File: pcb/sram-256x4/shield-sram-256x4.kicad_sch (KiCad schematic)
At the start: 24 parts, among them U1 IS61WV25616-10TLI, U2 IS61WV25616-10TLI, U3 IS61WV25616-10TLI, U4 IS61WV25616-10TLI

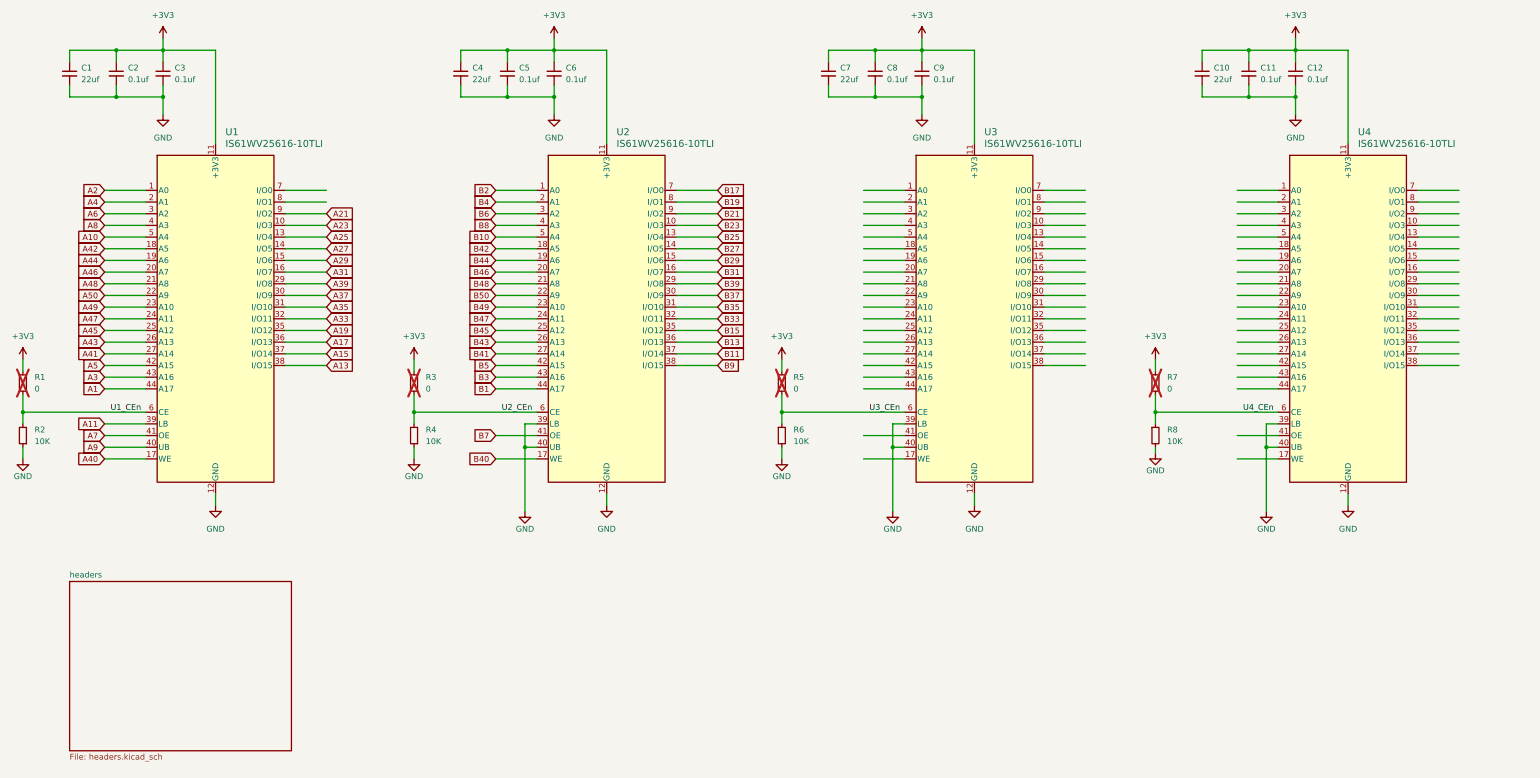
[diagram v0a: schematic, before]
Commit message: [pcb][sram-4x] all but pmod routed for adc board
The sram is doing double duty here during the cross over. It supports
the dfc stacking connector during the transition. It will be removed.
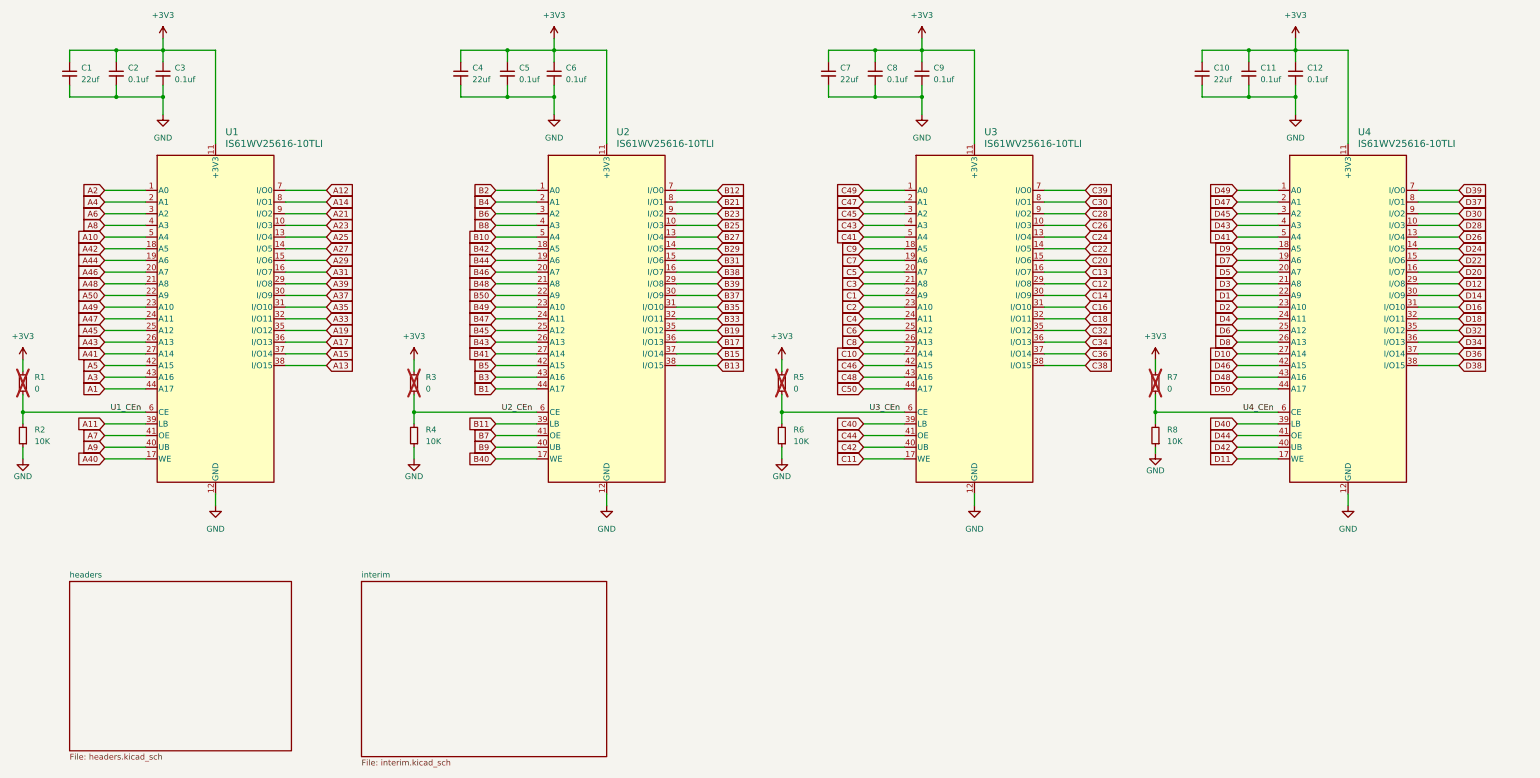
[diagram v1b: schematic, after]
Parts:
- U1, U2, U3, U4: footprint 44L_TSOP-2_400_ISI -> !Misc:44L_TSOP-2_400_ISI
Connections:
- net B11: now also U2.39 (LB); no longer U2.37 (I/O14)
- net B13: now also U2.38 (I/O15); no longer U2.36 (I/O13)
- net B15: now also U2.37 (I/O14); no longer U2.35 (I/O12)
- net B17: now also U2.36 (I/O13); no longer U2.7 (I/O0)
- net B19: now also U2.35 (I/O12); no longer U2.8 (I/O1)
- net B21: now also U2.8 (I/O1); no longer U2.9 (I/O2)
- net B23: now also U2.9 (I/O2); no longer U2.10 (I/O3)
- net B25: now also U2.10 (I/O3); no longer U2.13 (I/O4)
- net B27: now also U2.13 (I/O4); no longer U2.14 (I/O5)
- net B29: now also U2.14 (I/O5); no longer U2.15 (I/O6)
- net B31: now also U2.15 (I/O6); no longer U2.16 (I/O7)
- net B9: now also U2.40 (UB); no longer U2.38 (I/O15)
- net GND: now also R6.1, R8.1; no longer R6.2, R8.2, U2.39 (LB), U2.40 (UB), U3.39 (LB), U3.40 (UB), U4.39 (LB), U4.40 (UB)
- net U3_CEn: now also R6.2; no longer R6.1
- net U4_CEn: now also R8.2; no longer R8.1
- net C49: now reaches U3.1 (A0)
- net C26: now reaches U3.10 (I/O3)
- net C24: now reaches U3.13 (I/O4)
- net C22: now reaches U3.14 (I/O5)
- net C20: now reaches U3.15 (I/O6)
- net C13: now reaches U3.16 (I/O7)
- net C11: now reaches U3.17 (WE)
- net C9: now reaches U3.18 (A5)
- net C7: now reaches U3.19 (A6)
- net C47: now reaches U3.2 (A1)
- net C5: now reaches U3.20 (A7)
- net C3: now reaches U3.21 (A8)
- net C1: now reaches U3.22 (A9)
- net C2: now reaches U3.23 (A10)
- net C4: now reaches U3.24 (A11)
- net C6: now reaches U3.25 (A12)
- net C8: now reaches U3.26 (A13)
- net C10: now reaches U3.27 (A14)
- net C12: now reaches U3.29 (I/O8)
- net C45: now reaches U3.3 (A2)
- net C14: now reaches U3.30 (I/O9)
- net C16: now reaches U3.31 (I/O10)
- net C18: now reaches U3.32 (I/O11)
- net C32: now reaches U3.35 (I/O12)
- net C34: now reaches U3.36 (I/O13)
- net C36: now reaches U3.37 (I/O14)
- net C38: now reaches U3.38 (I/O15)
- net C43: now reaches U3.4 (A3)
- net C44: now reaches U3.41 (OE)
- net C46: now reaches U3.42 (A15)
- net C48: now reaches U3.43 (A16)
- net C50: now reaches U3.44 (A17)
- net C41: now reaches U3.5 (A4)
- net C39: now reaches U3.7 (I/O0)
- net C30: now reaches U3.8 (I/O1)
- net C28: now reaches U3.9 (I/O2)
- net D49: now reaches U4.1 (A0)
- net D28: now reaches U4.10 (I/O3)
- net D26: now reaches U4.13 (I/O4)
- net D24: now reaches U4.14 (I/O5)
- net D22: now reaches U4.15 (I/O6)
- net D20: now reaches U4.16 (I/O7)
- net D11: now reaches U4.17 (WE)
- net D9: now reaches U4.18 (A5)
- net D7: now reaches U4.19 (A6)
- net D47: now reaches U4.2 (A1)
- net D5: now reaches U4.20 (A7)
- net D3: now reaches U4.21 (A8)
- net D1: now reaches U4.22 (A9)
- net D2: now reaches U4.23 (A10)
- net D4: now reaches U4.24 (A11)
- net D6: now reaches U4.25 (A12)
- net D8: now reaches U4.26 (A13)
- net D10: now reaches U4.27 (A14)
- net D12: now reaches U4.29 (I/O8)
- net D45: now reaches U4.3 (A2)
- net D14: now reaches U4.30 (I/O9)
- net D16: now reaches U4.31 (I/O10)
- net D18: now reaches U4.32 (I/O11)
- net D32: now reaches U4.35 (I/O12)
- net D34: now reaches U4.36 (I/O13)
- net D36: now reaches U4.37 (I/O14)
- net D38: now reaches U4.38 (I/O15)
- net D43: now reaches U4.4 (A3)
- net D44: now reaches U4.41 (OE)
- net D46: now reaches U4.42 (A15)
- net D48: now reaches U4.43 (A16)
- net D50: now reaches U4.44 (A17)
- net D41: now reaches U4.5 (A4)
- net D39: now reaches U4.7 (I/O0)
- net D37: now reaches U4.8 (I/O1)
- net D30: now reaches U4.9 (I/O2)
- net A12: now reaches U1.7 (I/O0)
- net A14: now reaches U1.8 (I/O1)
- new net B12: U2.7 (I/O0)
- new net B38: U2.16 (I/O7)
- new net C40: U3.39 (LB)
- new net C42: U3.40 (UB)
- new net D40: U4.39 (LB)
- new net D42: U4.40 (UB)
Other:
- added sheet interim (interim.kicad_sch)
- moved on the sheet: R6, R8

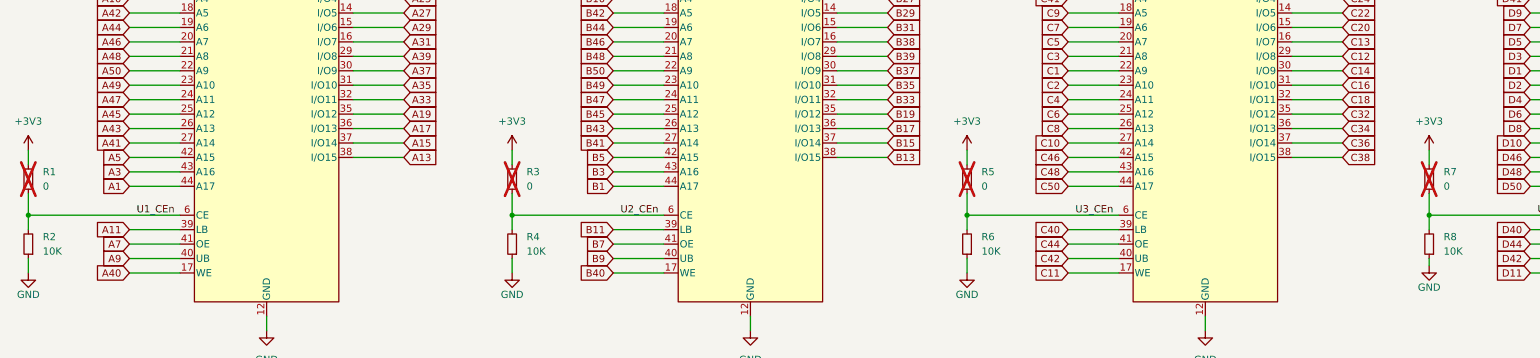
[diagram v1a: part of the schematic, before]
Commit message: [pcb] misc fixes during jlcpcb production submission
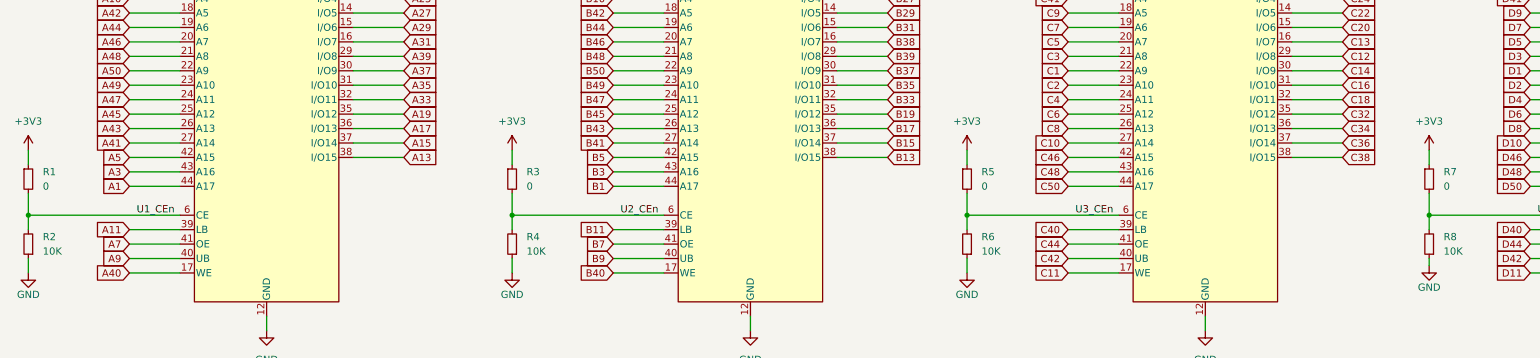
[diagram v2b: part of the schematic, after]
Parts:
- R1, R3, R5, R7: LCSC Part # C21189 -> DNP; now fitted
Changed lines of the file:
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@@
 		(in_bom yes)
 		(on_board yes)
-		(dnp yes)
+		(dnp no)
 		(fields_autoplaced yes)
 		(property "Reference" "R7"
@@
 			)
 		)
-		(property "LCSC Part #" "C21189"
+		(property "LCSC Part #" "DNP"
 			(at 265.43 100.33 0)
 			(effects
@@
 		(in_bom yes)
 		(on_board yes)
-		(dnp yes)
+		(dnp no)
 		(fields_autoplaced yes)
 		(property "Reference" "R5"
@@
 			)
 		)
-		(property "LCSC Part #" "C21189"
+		(property "LCSC Part #" "DNP"
 			(at 184.15 100.33 0)
 			(effects
@@
 		(in_bom yes)
 		(on_board yes)
-		(dnp yes)
+		(dnp no)
 		(fields_autoplaced yes)
 		(property "Reference" "R1"
@@
 			)
 		)
-		(property "LCSC Part #" "C21189"
+		(property "LCSC Part #" "DNP"
 			(at 19.05 100.33 0)
 			(effects
@@
 		(in_bom yes)
 		(on_board yes)
-		(dnp yes)
+		(dnp no)
 		(fields_autoplaced yes)
 		(property "Reference" "R3"
@@
 			)
 		)
-		(property "LCSC Part #" "C21189"
+		(property "LCSC Part #" "DNP"
 			(at 104.14 100.33 0)
 			(effects

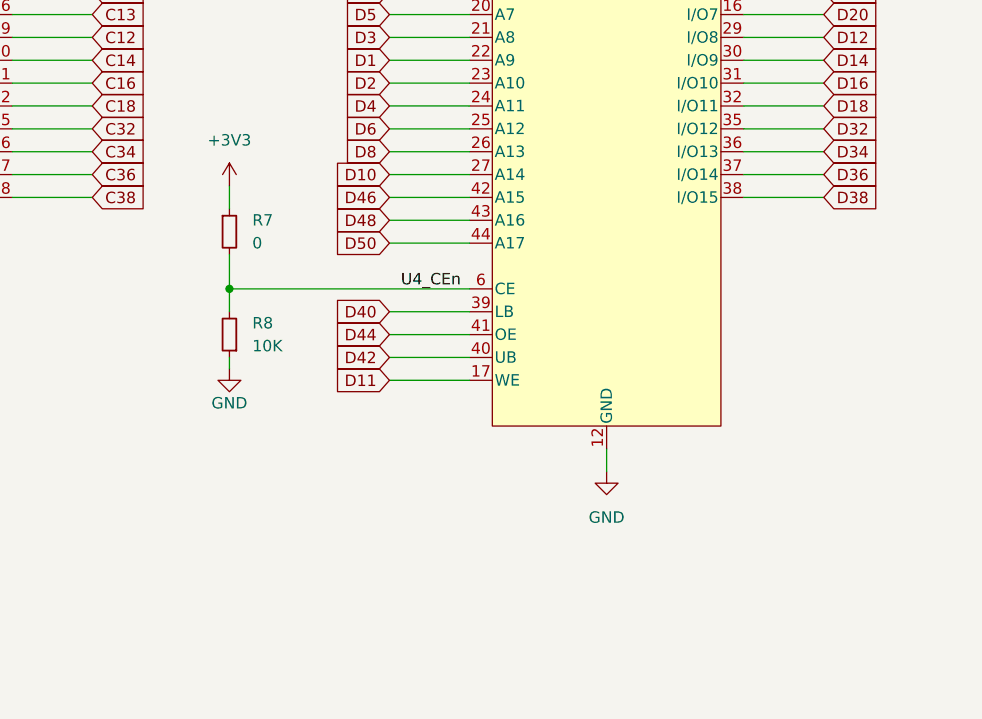
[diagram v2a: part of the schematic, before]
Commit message: [sram] attempted D signal issue work around
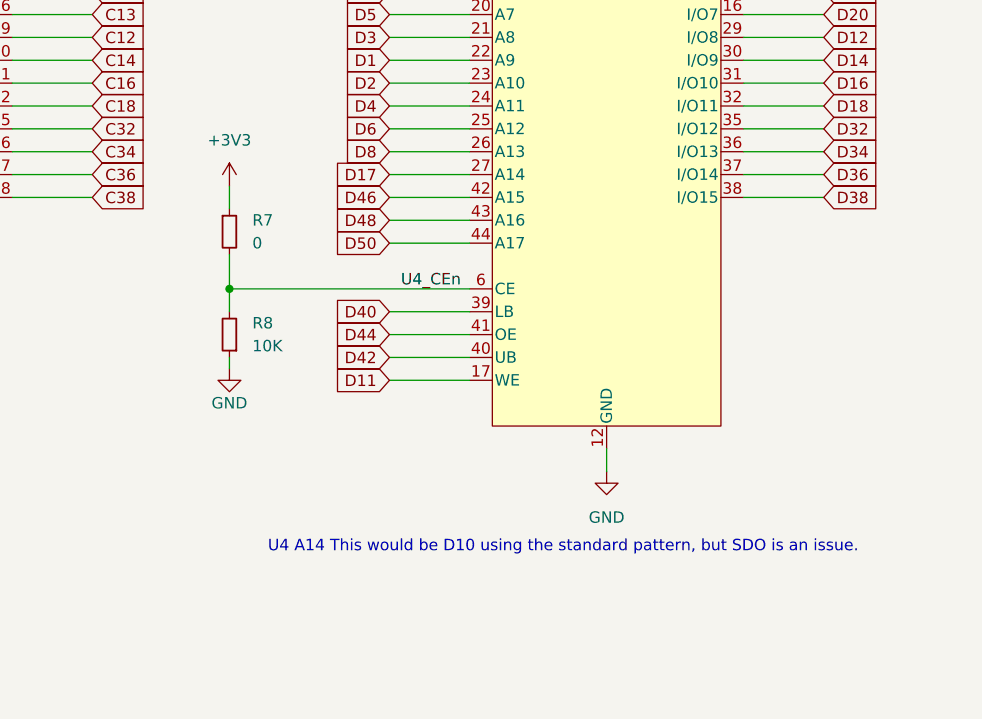
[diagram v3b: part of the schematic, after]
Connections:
- net D10 renamed D17
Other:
- note added: "U4 A14 This would be D10 using the standard pattern, but SDO is an issue."
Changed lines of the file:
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@@
 	(generator_version "9.0")
 	(paper "USLegal")
+	(text "U4 A14 This would be D10 using the standard pattern, but SDO is an issue.\n"
+		(exclude_from_sim no)
+		(at 302.514 135.382 0)
+		(effects
+			(font
+				(size 1.27 1.27)
+			)
+		)
+	)
 	(junction
 		(at 104.14 106.68)
@@
 		)
 	)
-	(global_label "D10"
+	(global_label "D17"
 		(shape input)
 		(at 283.21 93.98 180)
@@
 		)
 		(property "Intersheetrefs" "${INTERSHEET_REFS}"
-			(at 276.7172 93.98 0)
+			(at 276.5358 93.98 0)
 			(effects
 				(font
